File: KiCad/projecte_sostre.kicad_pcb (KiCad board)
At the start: 2 copper layers, 88 x 130 mm, 126 parts, among them J1 Conn_01x02, J10 DE9_Pins, J11 DE9_Pins, J2 Conn_01x05, J3 Conn_01x02, J4 Conn_01x02, J5 Conn_01x02, J6 Conn_01x02, J7 Screw_Terminal_01x02, J8 Screw_Terminal_01x02, J9 Screw_Terminal_01x02, SW1 SW_Push, SW2 SW_Push, SW3 SW_Push, SW4 SW_Push, SW5 SW_Push, SW6 SW_Push, U1 LM1117DT-3.3, U10 74AHCT125, U11 74AHCT125, U12 A1101xLH, U13 A1101xLH, U14 74AHCT125, U15 74AHCT125, U16 LM393, U17 LM393, U18 LM393, U19 LM393, U2 LM2596T-5, U20 LM393, U21 LM393, U3 L298N, U4 PIC24HJ128GP502, U5 INA219AxD, U6 INA219AxD, U7 MCP2561-E-MF, U8 MAX3232, U9 74AHCT125, Y1 Crystal

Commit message: pujo el esquematico a medio hacer despues de hacer cambios para mejorar el 2o layout
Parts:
- removed the REF** at (107.0, 145.0)
- removed the REF** at (186.0, 27.0)
- removed the REF** at (183.0, 147.0)
- removed the REF** at (106.0, 27.0)
- removed U15: 74AHCT125, Package_SO:SOIC-14_3.9x8.7mm_P1.27mm
- removed U16, U17, U18, U19, U20, U21: LM393, Package_SO:SOIC-8_5.3x6.2mm_P1.27mm
- removed U7: MCP2561-E-MF, Package_SO:SOIC-8-1EP_3.9x4.9mm_P1.27mm_EP2.29x3mm
- added C33: 100n, Capacitor_SMD:C_0805_2012Metric, F.Cu at (186.9, 85.3)
- added C34: 100n, Capacitor_SMD:C_0805_2012Metric, F.Cu at (185.9, 95.0)
- added C35: 100n, Capacitor_SMD:C_0805_2012Metric, F.Cu at (309.4, 85.3)
- added C36: 100n, Capacitor_SMD:C_0805_2012Metric, F.Cu at (270.3, 106.2)
- added C37: 100n, Capacitor_SMD:C_0805_2012Metric, F.Cu at (277.9, 128.0)
- added C38: 100n, Capacitor_SMD:C_0805_2012Metric, F.Cu at (278.9, 113.3)
- added D10: D, Diode_SMD:D_SMA, F.Cu at (264.2, 128.5)
- added D11: D, Diode_SMD:D_SMA, F.Cu at (264.2, 134.1)
- added D12: D, Diode_SMD:D_SMA, F.Cu at (251.0, 168.1)
- added D13: D, Diode_SMD:D_SMA, F.Cu at (251.0, 161.5)
- added D6: D, Diode_SMD:D_SMA, F.Cu at (270.8, 85.3)
- added D7: D, Diode_SMD:D_SMA, F.Cu at (266.2, 84.8)
- added D8: D, Diode_SMD:D_SMA, F.Cu at (266.2, 96.0)
- added D9: D, Diode_SMD:D_SMA, F.Cu at (272.3, 96.0)
- added REF**: MountingHole_2.1mm, MountingHole:MountingHole_2.1mm, F.Cu at (256.0, 73.7)
- added REF**: MountingHole_2.1mm, MountingHole:MountingHole_2.1mm, F.Cu at (248.9, 72.6)
- added REF**: MountingHole_2.1mm, MountingHole:MountingHole_2.1mm, F.Cu at (239.0, 63.2)
- added REF**: MountingHole_2.1mm, MountingHole:MountingHole_2.1mm, F.Cu at (238.8, 146.8)
- C13: value C -> 100n
- J1, J3, J4, J5, J6: footprint Connector_PinHeader_2.54mm:PinHeader_1x02_P2.54mm_Horizontal -> Connector_PinHeader_2.54mm:PinHeader_1x02_P2.54mm_Vertical
- J10, J11: footprint Connector_Dsub:DSUB-9_Socket_Horizontal_P2.77x2.84mm_EdgePinOffset4.94mm_Housed_MountingHolesOffset4.94mm -> Connector_Dsub:DSUB-9_Pins_Horizontal_P2.77x2.54mm_EdgePinOffset9.40mm
- R14: value 3.3k -> 10k
- R16: value 3.3k -> 20k
- R25: value 10k -> 20k
- SW1: moved to F.Cu
- U1: value LM1117DT-3.3 -> 74AHCT1G125; footprint Package_TO_SOT_SMD:TO-252-3_TabPin2 -> Package_TO_SOT_SMD:SOT-23-5_HandSoldering
- U10: value 74AHCT125 -> MCP2561-E-MF; footprint Package_SO:SOIC-14_3.9x8.7mm_P1.27mm -> Package_SO:SOIC-8-1EP_3.9x4.9mm_P1.27mm_EP2.29x3mm
- U11: value 74AHCT125 -> MAX3232; footprint Package_SO:SOIC-14_3.9x8.7mm_P1.27mm -> Package_SO:SOIC-16_3.9x9.9mm_P1.27mm
- U14: value 74AHCT125 -> L298P; footprint Package_SO:SOIC-14_3.9x8.7mm_P1.27mm -> Package_SO:HSOP-20-1EP_11.0x15.9mm_P1.27mm_SlugDown_ThermalVias
- U2: value LM2596T-5 -> LM393; footprint Package_TO_SOT_THT:TO-220-5_P3.4x3.7mm_StaggerOdd_Lead3.8mm_Vertical -> Package_SO:SOIC-8_3.9x4.9mm_P1.27mm
- U3: value L298N -> LM393; footprint Package_TO_SOT_THT:TO-220-15_P2.54x5.08mm_StaggerOdd_Lead4.58mm_Vertical -> Package_SO:SOIC-8_3.9x4.9mm_P1.27mm
- U5: value INA219AxD -> LM1117DT-3.3; footprint Package_SO:SOIC-8_3.9x4.9mm_P1.27mm -> Package_TO_SOT_SMD:TO-252-3_TabPin2
- U6: value INA219AxD -> LM2596T-5; footprint Package_SO:SOIC-8_3.9x4.9mm_P1.27mm -> Package_TO_SOT_THT:TO-220-5_P3.4x3.7mm_StaggerOdd_Lead3.8mm_Vertical
- U8: value MAX3232 -> INA219AxD; footprint Package_SO:SSOP-16_5.3x6.2mm_P0.65mm -> Package_SO:SOIC-8_3.9x4.9mm_P1.27mm
- U9: value 74AHCT125 -> INA219AxD; footprint Package_SO:SOIC-14_3.9x8.7mm_P1.27mm -> Package_SO:SOIC-8_3.9x4.9mm_P1.27mm
- Y1: footprint Crystal:Crystal_SMD_7050-2Pin_7.0x5.0mm_HandSoldering -> Crystal:Crystal_HC52-6mm_Vertical
- moved U14 302.1 mm to (260.6, 110.2), turned to -90 degrees
- moved J9 173.5 mm to (276.4, 118.1)
- moved J8 170.0 mm to (278.9, 92.2), turned to 90 degrees
- moved C18 143.8 mm to (270.3, 111.8), turned to -90 degrees
- moved R11 135.3 mm to (257.6, 120.9), turned to 0 degrees
- moved R12 128.6 mm to (257.6, 100.1)
- moved SW5 125.3 mm to (166.1, 147.3), turned to 180 degrees
- moved J7 121.9 mm to (224.2, 67.9), turned to 0 degrees
- moved D3 121.3 mm to (237.0, 83.6), turned to 90 degrees
- moved J5 119.5 mm to (171.2, 142.2), turned to 0 degrees
- moved SW4 119.2 mm to (155.7, 147.5)
- moved C13 116.3 mm to (231.9, 82.0)
- moved C7 110.8 mm to (154.4, 136.1)
- moved R6 109.8 mm to (154.4, 139.2), turned to 0 degrees
- moved C8 106.2 mm to (166.6, 138.7), turned to 0 degrees
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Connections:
- net /Power_Supply/Vbat renamed /Power_Supply/Vbat_before_D3
- net Net-(J1-Pin_2) renamed /Microprocesador/Conn_SW_M1_Max
- net Net-(J3-Pin_2) renamed /Microprocesador/Conn_SW_M1_Min
- net Net-(J4-Pin_2) renamed /Microprocesador/Conn_SW_M2_Max
- net Net-(J5-Pin_2) renamed /Microprocesador/Conn_SW_M2_Min
- net Net-(J6-Pin_2) renamed /Microprocesador/Conn_SW_LED_ON/OFF
- C12 pad 1: /Microprocesador/ON/OFF_LED -> ON/OFF_LED
- C13 pad 1: /Power_Supply/Vbat_after_D1 -> Vbat
- C23 pad 1: Net-(U8-C1+) -> Net-(U11-C1+)
- C23 pad 2: Net-(U8-C1-) -> Net-(U11-C1-)
- C26 pad 1: Net-(U8-C2+) -> Net-(U11-C2+)
- C26 pad 2: Net-(U8-C2-) -> Net-(U11-C2-)
- C27 pad 1: Net-(U8-VS+) -> Net-(U11-VS+)
- C27 pad 2: Net-(U8-VS-) -> Net-(U11-VS-)
- C29 pad 1: +3.3V -> 5V
- C30 pad 1: +3.3V -> 5V
- D2 pad 2: /Microprocesador/uC_programando? -> uC_programado?
- D3 pad 1: /Power_Supply/Vbat_after_D1 -> Vbat
- D4 pad 1: Net-(D4-K) -> /Power_Supply/entre_D3_y_L1
- J8 pad 1: /Power_Supply/M1_OUT1 -> M1_OUT2
- J8 pad 2: /Power_Supply/M1_OUT2 -> M1_OUT1
- J9 pad 1: /Power_Supply/M2_OUT1 -> M2_OUT2
- J9 pad 2: /Power_Supply/M2_OUT2 -> M2_OUT1
- L1 pad 1: Net-(D4-K) -> /Power_Supply/entre_D3_y_L1
- R14 pad 1: AVDD -> /Digital/SHall1_entre_Vout_y_Rdivisor
- R14 pad 2: I2C_SCL -> /Digital/VOUT_Hall1
- R16 pad 1: AVDD -> GND
- R16 pad 2: I2C_SDA -> /Digital/VOUT_Hall1
- R24 pad 1: +3.3V -> /Digital/SHall2_entre_Vout_y_Rdivisor
- R24 pad 2: /Digital/VOUT_Hall1 -> /Digital/VOUT_Hall2
- R25 pad 1: +3.3V -> GND
- R38 pad 1: /Digital/IN_LED -> /Digital/GPIO_3V3_a_5V
- R38 pad 2: /Digital/Adaptador_nivel_GPIO_de_3V3_a_5V -> /Digital/IN_LED
- R8 pad 2: /Microprocesador/ON/OFF_LED -> ON/OFF_LED
- SW6 pad 2: /Microprocesador/ON/OFF_LED -> ON/OFF_LED
- U1 pad 2: +3.3V -> LED_RGB
- U1 pad 3: 5V -> GND
- U10 pad 1: 5V -> CAN_TX
- U10 pad 3: unconnected-(U10-Pad3) -> +3.3V
- U10 pad 4: (no net) -> CAN_RX
- U10 pad 5: (no net) -> /Digital/SPLIT
- U10 pad 6: (no net) -> /Digital/CAN_L
- U10 pad 7: (no net) -> /Digital/CAN_H
- U10 pad 8: (no net) -> STBY_Trans_CAN
- U10 pad 9: (no net) -> GND
- U11 pad 1: 5V -> Net-(U11-C1+)
- U11 pad 10: (no net) -> unconnected-(U11-T2IN-Pad10)
- U11 pad 11: (no net) -> USART_TX
- U11 pad 12: (no net) -> MAX_RX
- U11 pad 13: (no net) -> USART_RX
- U11 pad 14: (no net) -> MAX_TX
- U11 pad 2: GND -> Net-(U11-VS+)
- U11 pad 3: unconnected-(U11-Pad3) -> Net-(U11-C1-)
- U11 pad 4: (no net) -> Net-(U11-C2+)
- U11 pad 5: (no net) -> Net-(U11-C2-)
- U11 pad 6: (no net) -> Net-(U11-VS-)
- U11 pad 7: (no net) -> unconnected-(U11-T2OUT-Pad7)
- U11 pad 8: (no net) -> unconnected-(U11-R2IN-Pad8)
- U11 pad 9: (no net) -> unconnected-(U11-R2OUT-Pad9)
- U12 pad 1: +3.3V -> 5V
- U12 pad 2: /Digital/VOUT_Hall1 -> /Digital/SHall1_entre_Vout_y_Rdivisor
- U13 pad 1: +3.3V -> 5V
- U13 pad 2: /Digital/VOUT_Hall2 -> /Digital/SHall2_entre_Vout_y_Rdivisor
- U14 pad 1: unconnected-(U14-Pad1) -> GND
- U14 pad 10: (no net) -> GND
- U14 pad 11: (no net) -> GND
- U14 pad 12: (no net) -> +3.3V
- U14 pad 13: (no net) -> INB1_M2
- U14 pad 14: (no net) -> /Power_Supply/ENABLE2
- U14 pad 2: unconnected-(U14-Pad2) -> SENSE_A
- U14 pad 4: (no net) -> M1_OUT1
- U14 pad 5: (no net) -> M1_OUT2
- U14 pad 6: (no net) -> Vbat
- U14 pad 7: (no net) -> INA1_M1
- U14 pad 8: (no net) -> /Power_Supply/ENABLE1
- U14 pad 9: (no net) -> INA2_M1
- U2 pad 1: /Power_Supply/Vbat_after_D1 -> DOWN_LOW_M1_Pos_Max
- U2 pad 2: Net-(D4-K) -> /Digital/VOUT_Hall1
- U2 pad 3: GND -> /Digital/Vref_1V_Max
- U2 pad 4: /Power_Supply/realimentación_buck_converter -> GND
- U2 pad 5: GND -> /Digital/VOUT_Hall1
- U3 pad 1: SENSE_A -> DOWN_LOW_M1_Pos_Min
- U3 pad 2: /Power_Supply/M1_OUT1 -> /Digital/VOUT_Hall2
- U3 pad 3: /Power_Supply/M1_OUT2 -> /Digital/Vref_1V_Min
- U3 pad 4: +12V -> GND
- U3 pad 5: INA1_M1 -> /Digital/VOUT_Hall2
- U3 pad 6: /Power_Supply/ENABLE1 -> /Digital/Vref_2,2V_Min
- U3 pad 7: INA2_M1 -> HIGH_UP_M1_Pos_Min
- U3 pad 8: GND -> +3.3V
- U4 pad 10: DOWN_LOW_M1_Pos_Max -> INB1_M2
- U4 pad 11: HIGH_UP_M1_Pos_Max -> INB2_M2
- U4 pad 12: /Microprocesador/ON/OFF_LED -> unconnected-(U4-RA10-Pad12)
- U4 pad 14: DOWN_LOW_M1_Pos_Min -> unconnected-(U4-RB14-Pad14)
- U4 pad 15: HIGH_UP_M1_Pos_Min -> unconnected-(U4-RB15-Pad15)
- U4 pad 19: LED_RGB -> unconnected-(U4-AN0/C12IN0-/RA0-Pad19)
- U4 pad 2: /Microprocesador/M1_go_Max -> unconnected-(U4-RC6-Pad2)
- U4 pad 20: INA2_M1 -> unconnected-(U4-AN1/C12IN1-/CTCMP/RA1-Pad20)
- U4 pad 21: INA1_M1 -> /Microprocesador/PGD
- U4 pad 22: STBY_Trans_CAN -> /Microprocesador/PGC
- U4 pad 23: USART_TX -> INA1_M1
- U4 pad 24: USART_RX -> INA2_M1
- U4 pad 25: /Microprocesador/uC_programando? -> DOWN_LOW_M1_Pos_Min
- U4 pad 26: unconnected-(U4-RC1-Pad26) -> HIGH_UP_M1_Pos_Min
- U4 pad 27: unconnected-(U4-RC2-Pad27) -> DOWN_LOW_M1_Pos_Max
- U4 pad 3: /Microprocesador/M1_go_Min -> uC_programado?
- U4 pad 32: unconnected-(U4-RA8-Pad32) -> HIGH_UP_M1_Pos_Max
- U4 pad 33: unconnected-(U4-RB4-Pad33) -> LED_RGB
- U4 pad 34: unconnected-(U4-NC-Pad34) -> STBY_Trans_CAN
- U4 pad 35: INB2_M2 -> ON/OFF_LED
- U4 pad 36: INB1_M2 -> CAN_RX
- U4 pad 37: unconnected-(U4-RC4-Pad37) -> CAN_TX
- U4 pad 38: Sensor_Hall -> /Microprocesador/M1_go_Max
- U4 pad 4: /Microprocesador/M2_go_Max -> unconnected-(U4-RC8-Pad4)
- U4 pad 41: unconnected-(U4-RB5/PGED3-Pad41) -> /Microprocesador/M1_go_Min
- U4 pad 42: unconnected-(U4-RB6/PGEC3-Pad42) -> /Microprocesador/M2_go_Max
- U4 pad 43: unconnected-(U4-RB7-Pad43) -> /Microprocesador/M2_go_Min
- U4 pad 5: /Microprocesador/M2_go_Min -> unconnected-(U4-RC9-Pad5)
- U4 pad 8: /Microprocesador/PGD -> USART_TX
- U4 pad 9: /Microprocesador/PGC -> USART_RX
- U5 pad 2: GND -> +3.3V
- U5 pad 3: I2C_SDA -> 5V
- U6 pad 1: GND -> Vbat
- U6 pad 2: AVDD -> /Power_Supply/entre_D3_y_L1
- U6 pad 3: I2C_SDA -> GND
- U6 pad 4: I2C_SCL -> /Power_Supply/realimentación_buck_converter
- U6 pad 5: AVDD -> GND
- U8 pad 1: Net-(U8-C1+) -> GND
- U8 pad 2: Net-(U8-VS+) -> GND
- U8 pad 3: Net-(U8-C1-) -> I2C_SDA
- U8 pad 4: Net-(U8-C2+) -> I2C_SCL
- U8 pad 5: Net-(U8-C2-) -> AVDD
- U8 pad 6: Net-(U8-VS-) -> GND
- U8 pad 7: unconnected-(U8-T2OUT-Pad7) -> /Analogica/IN-
- U8 pad 8: unconnected-(U8-R2IN-Pad8) -> /Analogica/IN+
- U9 pad 1: 5V -> GND
- U9 pad 2: GND -> AVDD
- U9 pad 3: unconnected-(U9-Pad3) -> I2C_SDA
- U9 pad 4: (no net) -> I2C_SCL
- U9 pad 5: (no net) -> AVDD
- U9 pad 6: (no net) -> GND
- U9 pad 7: (no net) -> /Analogica/IN-
- U9 pad 8: (no net) -> /Analogica/IN+
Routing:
- net +3.3V: track 414.6 -> 17.2 mm, vias 32 -> 0
- net 5V: track 178.8 -> 38.0 mm, vias 9 -> 0
- net M1_OUT2: track 0.00 -> 105.1 mm
- net STBY_Trans_CAN: track 87.8 -> 4.18 mm, vias 2 -> 1
- net USART_TX: track 122.5 -> 40.7 mm, vias 2 -> 0
- net GND: track 150.2 -> 226.0 mm, vias 61 -> 196
- net M1_OUT1: track 0.00 -> 70.3 mm
- net USART_RX: track 108.9 -> 42.8 mm, vias 2 -> 0
- net /Microprocesador/PGC: track 64.1 -> 4.23 mm
- net /Microprocesador/PGD: track 65.2 -> 7.10 mm
- net /Analogica/IN+: track 68.2 -> 13.9 mm
- net M2_OUT2: track 0.00 -> 46.6 mm
- net /Analogica/IN-: track 56.7 -> 11.6 mm, vias 2 -> 0
- net INB2_M2: track 22.5 -> 66.9 mm
- net /Microprocesador/ON/OFF_LED: track 43.0 -> 0.00 mm
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- added copper zone on F.Cu, net (none)
- added copper zone on F.Cu, net 5V
- added copper zone on F.Cu, net GND
- added copper zone on F.Cu, net Vbat
- removed copper zone on B.Cu, net GND
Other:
- board size 88 x 130 mm -> 111.2 x 89.4 mm
- board text added: "3V3 o 5V"
- board text added: "GND Power"
- board text added: "GND normal"
- board text added: "K"
- board text added: "señales digitales"

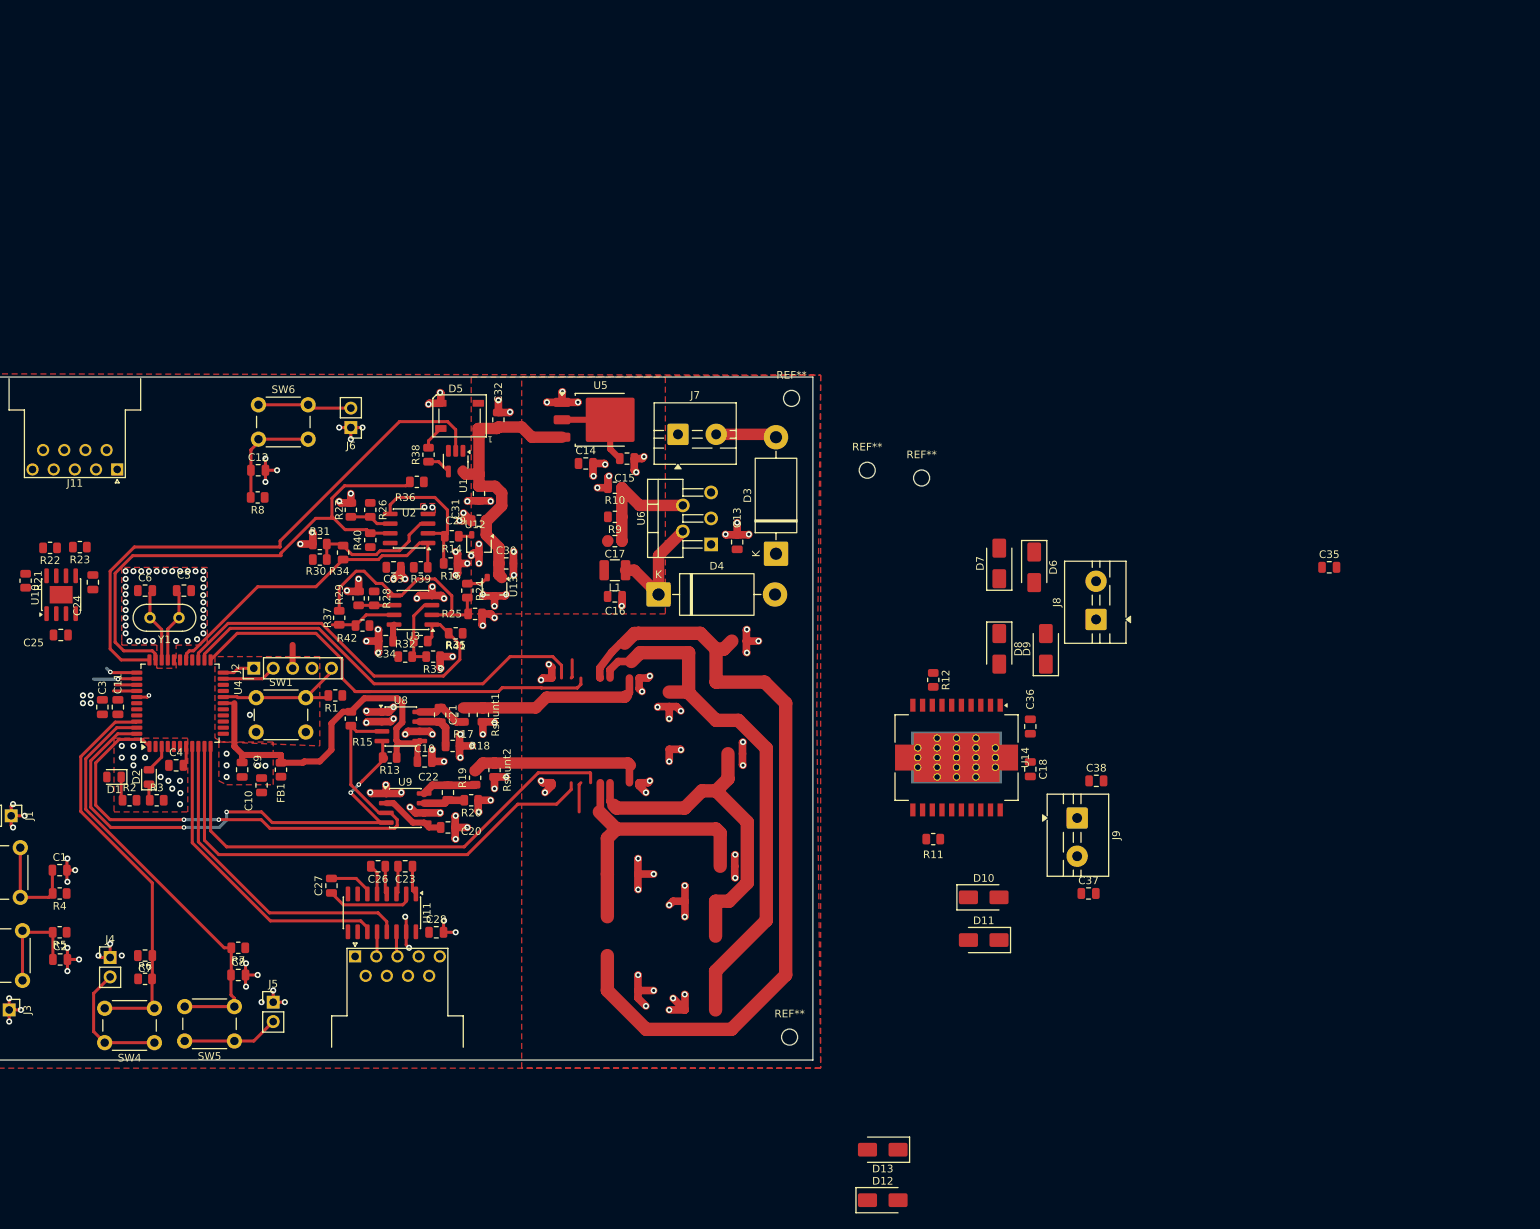
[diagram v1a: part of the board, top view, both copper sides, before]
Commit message: Test Points y Parte POwer ruteada de nuevo
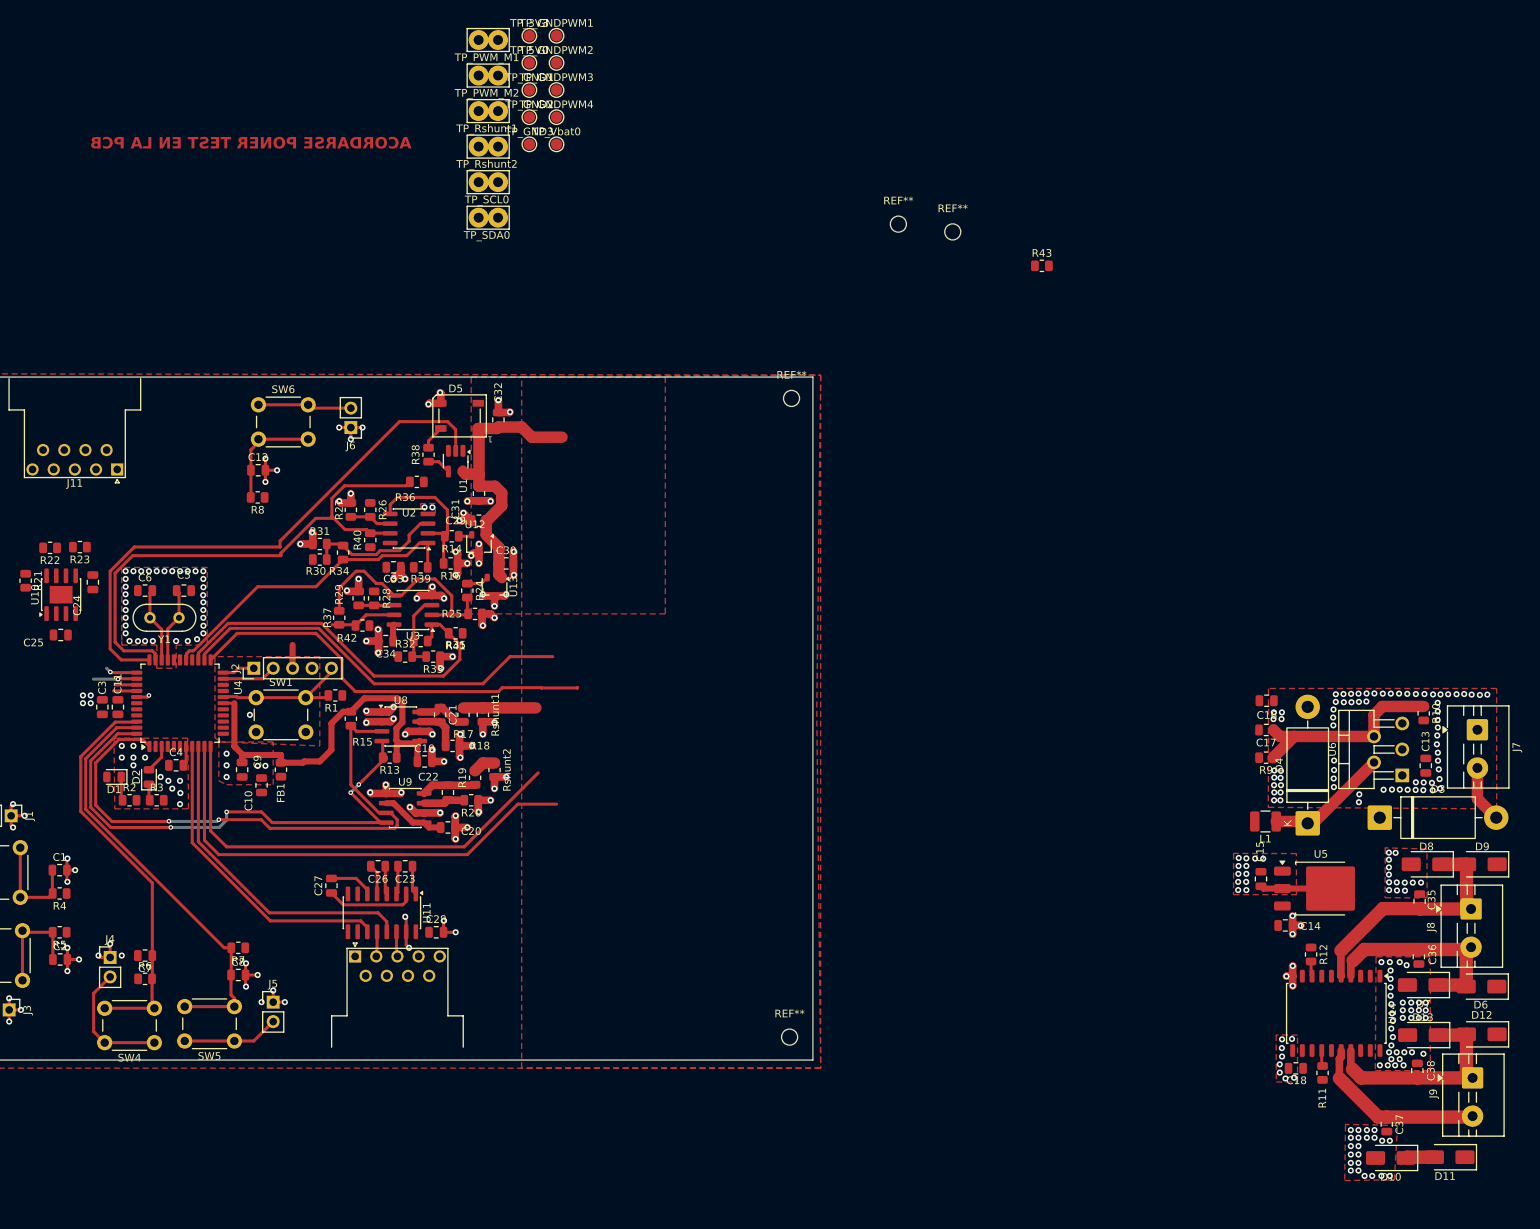
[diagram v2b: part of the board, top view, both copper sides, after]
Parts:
- added R43: 0, Resistor_SMD:R_0805_2012Metric, F.Cu at (271.8, 45.9)
- added TP_3V3: TestPoint, TestPoint:TestPoint_Pad_D1.5mm, F.Cu at (204.7, 15.8)
- added TP_5V0: TestPoint, TestPoint:TestPoint_Pad_D1.5mm, F.Cu at (204.7, 19.4)
- added TP_GND1: TestPoint, TestPoint:TestPoint_Pad_D1.5mm, F.Cu at (204.7, 22.9)
- added TP_GND2: TestPoint, TestPoint:TestPoint_Pad_D1.5mm, F.Cu at (204.7, 26.4)
- added TP_GND3: TestPoint, TestPoint:TestPoint_Pad_D1.5mm, F.Cu at (204.7, 30.0)
- added TP_GNDPWM1: TestPoint, TestPoint:TestPoint_Pad_D1.5mm, F.Cu at (208.3, 15.8)
- added TP_GNDPWM2: TestPoint, TestPoint:TestPoint_Pad_D1.5mm, F.Cu at (208.3, 19.4)
- added TP_GNDPWM3: TestPoint, TestPoint:TestPoint_Pad_D1.5mm, F.Cu at (208.3, 22.9)
- added TP_GNDPWM4: TestPoint, TestPoint:TestPoint_Pad_D1.5mm, F.Cu at (208.3, 26.4)
- added TP_PWM_M1: TestPoint_2Pole, TestPoint:TestPoint_Bridge_Pitch2.54mm_Drill1.3mm, F.Cu at (198.1, 16.4)
- added TP_PWM_M2: TestPoint_2Pole, TestPoint:TestPoint_Bridge_Pitch2.54mm_Drill1.3mm, F.Cu at (198.1, 21.0)
- added TP_Rshunt1: TestPoint_2Pole, TestPoint:TestPoint_Bridge_Pitch2.54mm_Drill1.3mm, F.Cu at (198.1, 25.6)
- added TP_Rshunt2: TestPoint_2Pole, TestPoint:TestPoint_Bridge_Pitch2.54mm_Drill1.3mm, F.Cu at (198.1, 30.3)
- added TP_SCL0: TestPoint_2Pole, TestPoint:TestPoint_Bridge_Pitch2.54mm_Drill1.3mm, F.Cu at (198.1, 35.0)
- added TP_SDA0: TestPoint_2Pole, TestPoint:TestPoint_Bridge_Pitch2.54mm_Drill1.3mm, F.Cu at (198.1, 39.6)
- added TP_Vbat0: TestPoint, TestPoint:TestPoint_Pad_D1.5mm, F.Cu at (208.3, 30.0)
- U14: footprint Package_SO:HSOP-20-1EP_11.0x15.9mm_P1.27mm_SlugDown_ThermalVias -> Package_SO:Infineon_SOIC-20W_7.6x12.8mm_P1.27mm
- moved U5 112.5 mm to (308.3, 127.4)
- moved J7 111.5 mm to (328.8, 106.6), turned to -90 degrees
- moved R10 109.9 mm to (321.7, 104.5), turned to -90 degrees
- moved C14 109.7 mm to (303.6, 132.2)
- moved C15 99.5 mm to (300.4, 126.1), turned to 90 degrees
- moved U6 95.4 mm to (318.9, 112.6)
- moved C13 94.7 mm to (322.0, 111.3)
- moved L1 91.3 mm to (301.0, 118.6)
- moved R9 90.8 mm to (301.1, 110.2)
- moved D4 90.1 mm to (306.6, 118.8), turned to 90 degrees
- moved C17 88.7 mm to (301.1, 106.6)
- moved C16 86.4 mm to (301.2, 102.8)
- moved D3 86.2 mm to (316.0, 118.1), turned to 0 degrees
- moved D12 81.3 mm to (329.3, 146.4), turned to 180 degrees
- moved D6 80.2 mm to (329.3, 140.2), turned to 180 degrees
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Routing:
- net M1_OUT2: track 105.1 -> 32.0 mm
- net GND: track 226.0 -> 154.5 mm, vias 196 -> 318
- net M1_OUT1: track 70.3 -> 27.5 mm
- net SENSE_B: track 23.2 -> 2.96 mm
- net M2_OUT2: track 46.6 -> 28.5 mm
- net SENSE_A: track 24.4 -> 9.48 mm
- net /Power_Supply/realimentación_buck_converter: track 15.9 -> 27.2 mm
- net M2_OUT1: track 37.1 -> 27.1 mm
- net INB2_M2: track 66.9 -> 58.8 mm
- net INB1_M2: track 65.5 -> 61.9 mm
- net INA2_M1: track 55.5 -> 52.2 mm
- net +3.3V: track 17.2 -> 14.5 mm
- net /Power_Supply/ENABLE2: track 3.91 -> 2.07 mm
- net INA1_M1: track 57.8 -> 56.3 mm
- net /Power_Supply/entre_D3_y_L1: track 15.2 -> 16.2 mm
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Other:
- board text added: "ACORDARSE PONER TEST EN LA PCB"
- board text removed: "K"
